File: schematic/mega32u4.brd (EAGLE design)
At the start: 44.4 x 42 mm, 28 parts, among them Q1 16 MHz, T1 BC847, X1 MINI-USB-32005-201

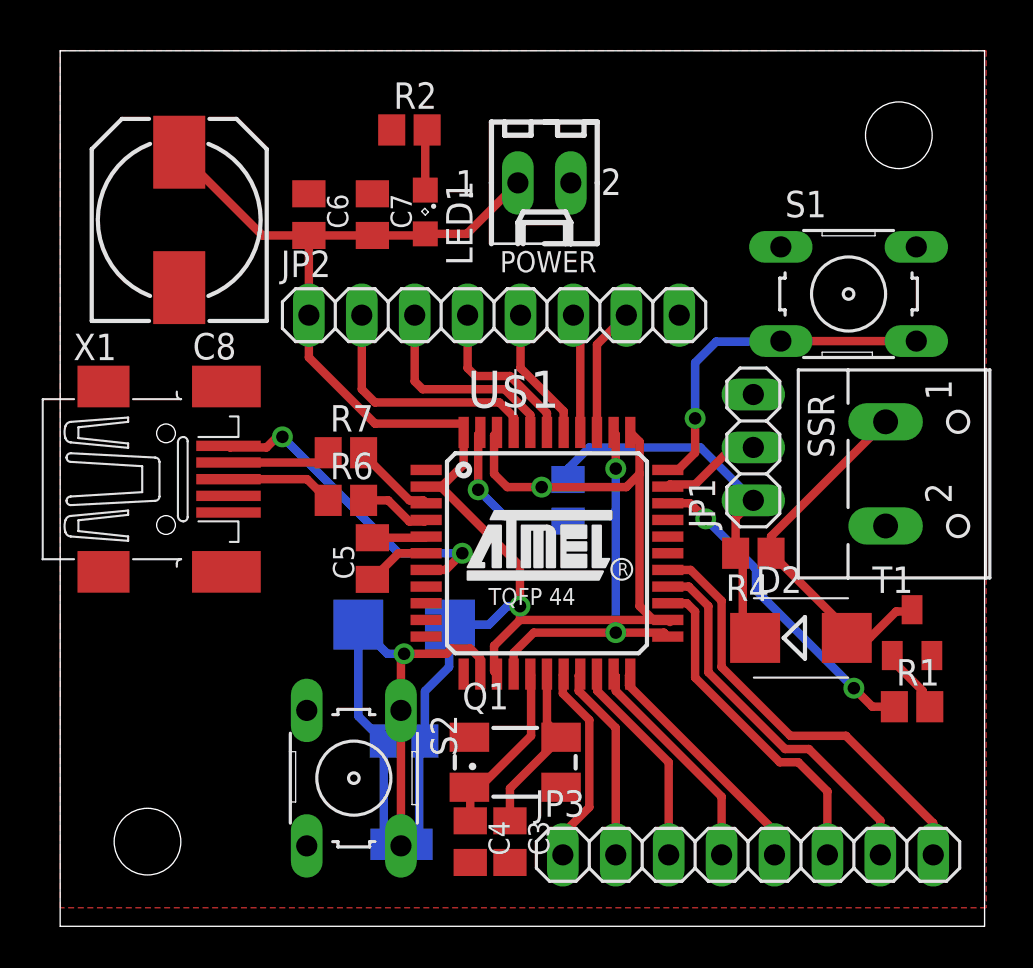
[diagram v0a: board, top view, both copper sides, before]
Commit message: Design Rule Check applied and errors corrected
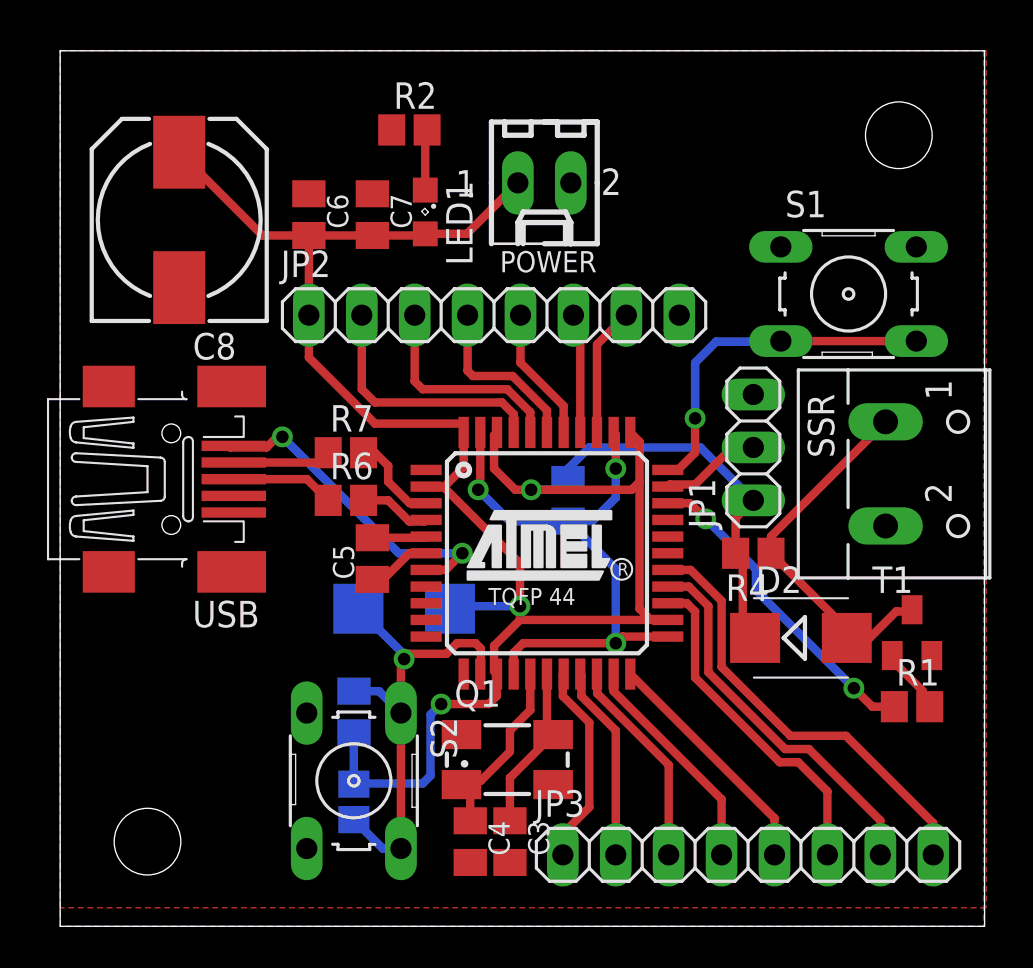
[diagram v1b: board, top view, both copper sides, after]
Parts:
- removed X1: MINI-USB-32005-201, con-cypressindustries:32005-201
- added USB: (no value), con-cypressindustries:32005-201
- U$1: value ATMEGA32U4-AU -> ATMEGA32U4
- moved R5 3.06 mm to (40.3, 24.9), turned to 270 degrees
- moved C1 2.79 mm to (40.3, 29.2), turned to 90 degrees
- moved D1 0.76 mm to (42.7, 34.2)
- moved Q1 0.40 mm to (47.6, 26.9)
- moved S2 0.13 mm to (40.3, 25.9)
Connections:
- removed net N$11: X1.4
- net GND: now also USB.5; no longer X1.5
- net UDM: now also USB.2; no longer X1.2
- net UDP: now also USB.3; no longer X1.3
- net VBUS: now also USB.1; no longer X1.1
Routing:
- net RESET: track 27.8 -> 23.4 mm
- net VCC: track 110.1 -> 112.8 mm, vias 2 -> 3
- net N$3: track 8.63 -> 9.53 mm
- net N$2: track 8.83 -> 8.14 mm
- added copper zone on layer 16, net GND

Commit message: RGB-Led added, pin header repositioned, mounting holes added, ...
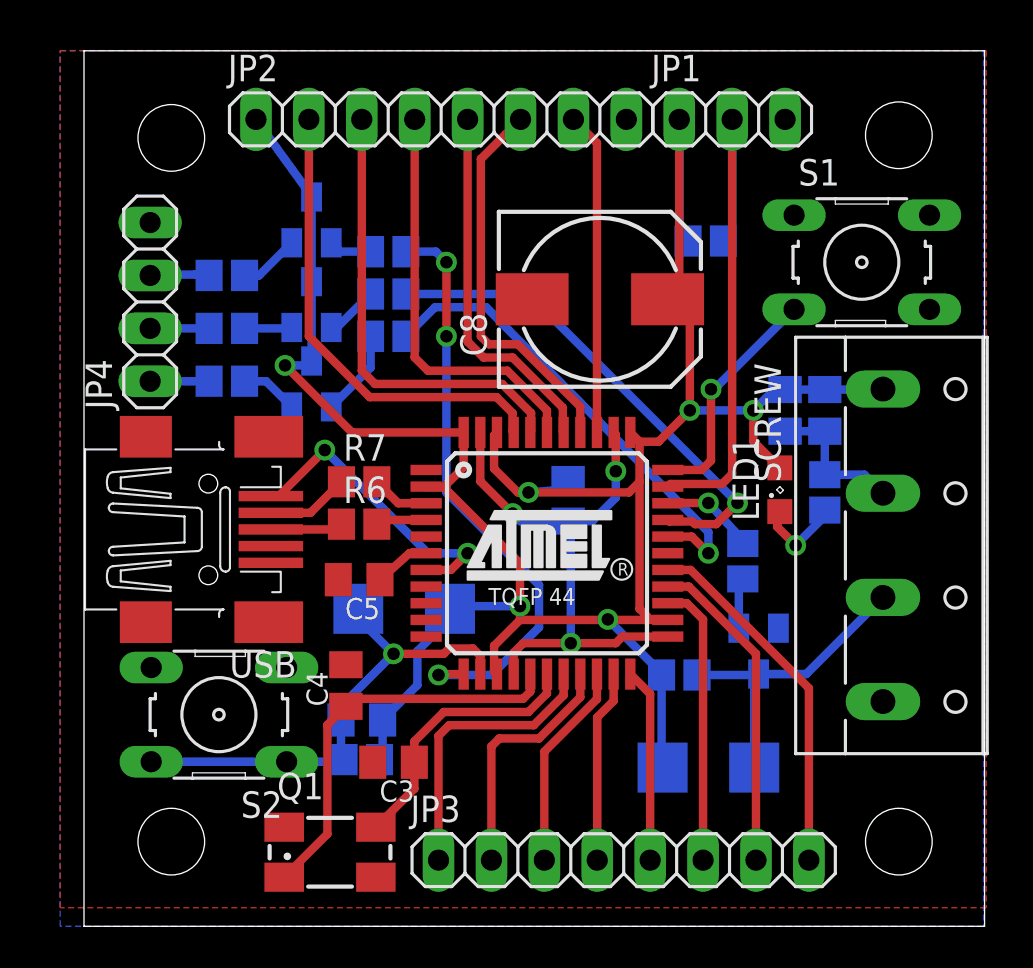
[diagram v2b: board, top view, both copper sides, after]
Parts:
- removed POWER: 22-27-2021-02, con-molex:6410-02
- removed SSR: (no value), con-wago-500:W237-102
- added JP4: (no value), pinhead:1X04
- added R10: 4k7, resistor:R0805
- added R11, R12: 56, resistor:R0805
- added R13: 1k2, resistor:R0805
- added R3, R8, R9: 1k5, resistor:R0805
- added SCREW: (no value), con-wago-500:W237-4
- added T2, T3, T4: (no value), transistor-neu-to92:SOT23-BEC
- R2: value 10K -> 220
- moved C6 26.5 mm to (62.9, 43.7), flipped to the bottom, turned to 90 degrees
- moved R2 26.5 mm to (62.9, 39.8), flipped to the bottom, turned to 270 degrees
- moved C7 21.9 mm to (61.0, 43.7), flipped to the bottom, turned to 90 degrees
- moved LED1 21.6 mm to (60.7, 39.9), turned to 90 degrees
- moved C8 20.5 mm to (52.1, 49.0), turned to 0 degrees
- moved JP1 15.8 mm to (58.4, 57.7), turned to 0 degrees
- moved R1 10.7 mm to (58.9, 36.4), flipped to the bottom, turned to 270 degrees
- moved JP2 9.74 mm to (44.5, 57.7)
- moved Q1 9.60 mm to (39.1, 22.5)
- moved C4 9.58 mm to (39.9, 30.5), turned to 90 degrees
- moved D2 7.65 mm to (57.3, 26.5), flipped to the bottom, turned to 180 degrees
- moved T1 7.42 mm to (59.7, 32.1), flipped to the bottom, turned to 180 degrees
- moved S2 7.21 mm to (33.8, 29.1), turned to 180 degrees
- moved R4 6.84 mm to (55.9, 31.0), flipped to the bottom, turned to 0 degrees
- moved C3 6.76 mm to (42.2, 26.8), turned to 180 degrees
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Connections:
- new net LEDB: R9.2, U$1.12
- new net LEDB_CON: JP4.3, R11.1
- new net LEDG: R3.2, U$1.30
- new net LEDG_CON: JP4.2, R12.1
- new net LEDR: R8.2, U$1.29
- new net LEDR_CON: JP4.1, R13.1
- new net N$11: R9.1, T4.B
- new net N$14: R11.2, T4.E
- new net N$15: R12.2, T3.E
- new net N$16: R13.2, T2.E
- new net N$8: R8.1, T2.B
- new net SSR-VCC: D2.A, R4.1, SCREW.3, T1.3
- net 1WIRE: now also R10.1
- net GND: now also JP4.4, SCREW.2, SCREW.4; no longer POWER.2, SSR.2
- net N$9: now also R3.1, T3.B; no longer D2.A, R4.1, SSR.1, T1.3
- net VCC: now also R10.2, SCREW.1, T2.C, T3.C, T4.C; no longer POWER.1
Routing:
- net LEDB: track 0.00 -> 28.5 mm, vias 0 -> 3
- net LEDG: track 0.00 -> 23.9 mm, vias 0 -> 1
- net LEDR: track 0.00 -> 22.9 mm, vias 0 -> 1
- net 1WIRE: track 4.88 -> 26.4 mm
- net N$9: track 17.9 -> 2.55 mm
- net SSR-VCC: track 0.00 -> 15.0 mm
- net PF6: track 5.77 -> 18.6 mm
- net VCC: track 112.8 -> 125.1 mm, vias 3 -> 6
- net PF1: track 10.3 -> 22.0 mm
- net PF4: track 8.32 -> 19.9 mm
- net PF5: track 6.49 -> 17.8 mm
- net SSR: track 15.5 -> 4.54 mm, vias 2 -> 1
- net PF0: track 12.2 -> 22.7 mm
- net N$3: track 9.53 -> 19.4 mm
- net PF7: track 6.21 -> 15.5 mm
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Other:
- board size 44.4 x 42 mm -> 43.2 x 42 mm

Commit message: Labels modified
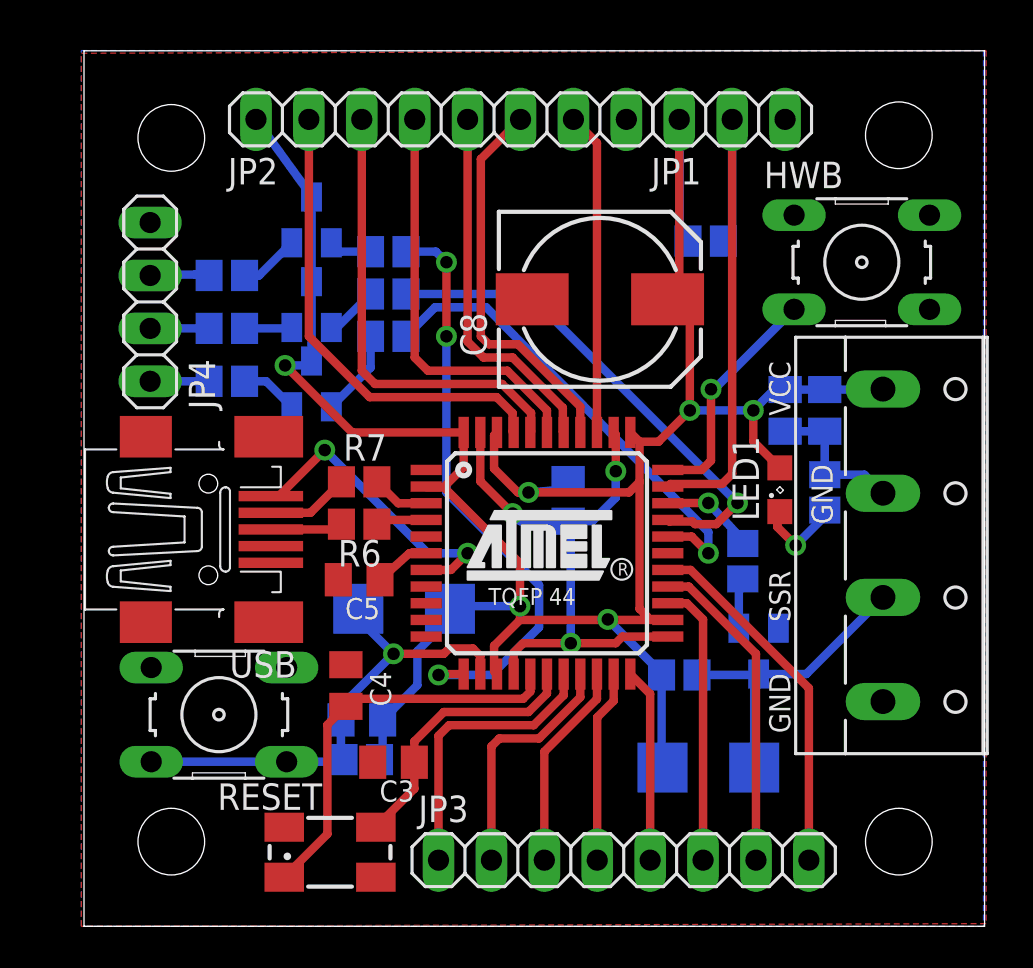
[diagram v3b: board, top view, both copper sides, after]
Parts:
- T1: value BC847 -> (none); device transistor:SOT23 -> transistor-neu-to92:SOT23-BEC
- renumbered S1 to HWB, S2 to RESET
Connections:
- net GND: now also T1.E; no longer T1.2
- net N$5: now also T1.B; no longer T1.1
- net SSR-VCC: now also T1.C; no longer T1.3
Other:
- board text added: "GND"
- board text added: "SSR"
- board text added: "VCC"

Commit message: minor changes
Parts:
- removed LED1: (no value), led:SML0805
- added POWER: (no value), led:SML0805
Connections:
- net N$13: now also POWER.C; no longer LED1.C
- net VCC: now also POWER.A; no longer LED1.A
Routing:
- net N$10: track 11.3 -> 17.8 mm
- net N$13: track 4.23 -> 6.38 mm
- net GND: vias 0 -> 1
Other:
- board text added: "+5V"
- board text added: "ChaosCoffeeControl"
- board text added: "v0.1"
- board text removed: "VCC"
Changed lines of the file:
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@@
 <layer number="45" name="Holes" color="7" fill="1" visible="yes" active="yes"/>
 <layer number="46" name="Milling" color="3" fill="1" visible="no" active="yes"/>
-<layer number="47" name="Measures" color="7" fill="1" visible="no" active="yes"/>
+<layer number="47" name="Measures" color="7" fill="1" visible="yes" active="yes"/>
 <layer number="48" name="Document" color="7" fill="1" visible="yes" active="yes"/>
 <layer number="49" name="Reference" color="7" fill="1" visible="yes" active="yes"/>
@@
 <hole x="31.496" y="56.769" drill="3.2"/>
 <hole x="66.421" y="22.987" drill="3.2"/>
-<dimension x1="27.305" y1="60.95" x2="27.305" y2="18.923" x3="22.86" y3="39.9365" layer="1"/>
-<dimension x1="27.305" y1="18.923" x2="70.536" y2="18.923" x3="48.9205" y3="63.246" layer="1"/>
-<text x="61.214" y="43.434" size="1.016" layer="25" rot="R90">VCC</text>
+<dimension x1="27.305" y1="60.95" x2="27.305" y2="18.923" x3="22.86" y3="39.9365" layer="47"/>
+<dimension x1="27.305" y1="18.923" x2="70.536" y2="18.923" x3="48.9205" y3="63.246" layer="47"/>
+<text x="61.214" y="43.942" size="1.016" layer="25" rot="R90">+5V</text>
 <text x="61.214" y="28.194" size="1.016" layer="25" rot="R90">GND</text>
 <text x="61.214" y="33.528" size="1.016" layer="25" rot="R90">SSR</text>
-<text x="63.246" y="38.227" size="1.016" layer="25" rot="R90">GND</text>
+<text x="61.214" y="36.957" size="1.016" layer="25" rot="R90">GND</text>
+<text x="46.609" y="25.4" size="1.27" layer="51">ChaosCoffeeControl</text>
+<text x="52.705" y="24.13" size="1.016" layer="51">v0.1</text>
 </plain>
 <attributes>
@@
 </autorouter>
 <elements>
-<element name="U$1" library="mega32U4" package="TQFP44" value="ATMEGA32U4" x="49.53" y="36.83" smashed="yes">
-<attribute name="VALUE" x="43.688" y="43.6959" size="1.27" layer="27"/>
-</element>
+<element name="U$1" library="mega32U4" package="TQFP44" value="ATMEGA32U4" x="49.53" y="36.83" smashed="yes"/>
 <element name="C1" library="resistor" package="C0805K" value="47nF" x="40.64" y="28.829" smashed="yes" rot="MR0">
 <attribute name="NAME" x="41.64" y="29.704" size="1.016" layer="26" rot="MR0"/>
@@
 <attribute name="MF" value="" x="39.116" y="22.479" size="1.778" layer="27" display="off"/>
 <attribute name="OC_FARNELL" value="unknown" x="39.116" y="22.479" size="1.778" layer="27" display="off"/>
-<attribute name="VALUE" x="35.814" y="21.844" size="1.27" layer="27"/>
 </element>
 <element name="USB" library="con-cypressindustries" package="32005-201" value="" x="33.274" y="37.973" smashed="yes">
@@
 <attribute name="MF" value="" x="33.274" y="37.973" size="1.778" layer="27" display="off"/>
 <attribute name="OC_FARNELL" value="unknown" x="33.274" y="37.973" size="1.778" layer="27" display="off"/>
-<attribute name="NAME" x="34.29" y="30.861" size="1.27" layer="25"/>
+<attribute name="NAME" x="31.369" y="32.385" size="1.27" layer="25"/>
 <attribute name="VALUE" x="28.829" y="30.988" size="1.27" layer="27"/>
 </element>
@@
 <attribute name="MF" value="" x="33.782" y="29.083" size="1.778" layer="27" rot="R180" display="off"/>
 <attribute name="OC_FARNELL" value="176432" x="33.782" y="29.083" size="1.778" layer="27" rot="R180" display="off"/>
-<attribute name="NAME" x="38.735" y="25.781" size="1.27" layer="25" ratio="10" rot="R180"/>
+<attribute name="NAME" x="39.37" y="25.781" size="1.27" layer="25" ratio="10" rot="R180"/>
 <attribute name="VALUE" x="36.83" y="34.163" size="1.27" layer="27" ratio="10" rot="R180"/>
 </element>
@@
 <attribute name="NAME" x="63.74" y="42.688" size="1.016" layer="26" rot="MR90"/>
 </element>
-<element name="LED1" library="led" package="SML0805" value="" x="60.706" y="39.878" rot="R90"/>
+<element name="POWER" library="led" package="SML0805" value="" x="60.706" y="42.037" smashed="yes" rot="R90">
+<attribute name="NAME" x="59.706" y="39.267" size="1.27" layer="25" rot="R90"/>
+<attribute name="VALUE" x="62.706" y="40.537" size="1.27" layer="27" rot="R90"/>
+</element>
 <element name="C8" library="resistor" package="150CLZ-0810" value="470uF" x="52.07" y="49.022"/>
 <element name="C7" library="resistor" package="C0805K" value="330nF" x="60.96" y="43.688" smashed="yes" rot="MR90">
@@
 <wire x1="50.292" y1="39.878" x2="48.641" y2="39.751" width="0.4064" layer="16"/>
 <via x="48.641" y="39.751" extent="1-16" drill="0.6"/>
-<contactref element="LED1" pad="A"/>
+<contactref element="POWER" pad="A"/>
 <contactref element="C8" pad="+"/>
 <contactref element="C6" pad="2"/>
@@
 <via x="59.436" y="43.688" extent="1-16" drill="0.6"/>
 <wire x1="59.436" y1="43.688" x2="59.436" y2="42.198" width="0.4064" layer="1"/>
-<wire x1="59.436" y1="42.198" x2="60.706" y2="40.928" width="0.4064" layer="1"/>
+<wire x1="59.436" y1="42.198" x2="60.706" y2="43.087" width="0.4064" layer="1"/>
 <wire x1="60.96" y1="44.688" x2="60.436" y2="44.688" width="0.4064" layer="16"/>
 <wire x1="59.436" y1="43.688" x2="56.388" y2="43.688" width="0.4064" layer="16"/>
@@
 <contactref element="JP4" pad="4"/>
 <contactref element="T1" pad="E"/>
+<via x="52.451" y="36.068" extent="1-16" drill="0.6"/>
 </signal>
 <signal name="N$4">
@@
 <wire x1="57.404" y1="44.704" x2="57.5564" y2="44.704" width="0.4064" layer="16"/>
 <wire x1="57.5564" y1="44.704" x2="61.3918" y2="48.5394" width="0.4064" layer="16"/>
-<wire x1="61.3918" y1="48.5394" x2="67.8942" y2="48.5394" width="0" layer="19" extent="1-1"/>
+<wire x1="61.3918" y1="48.5394" x2="67.8942" y2="48.5394" width="0.4064" layer="16"/>
 </signal>
 <signal name="PF7">
@@
 <signal name="N$13">
 <contactref element="R2" pad="2"/>
-<contactref element="LED1" pad="C"/>
-<wire x1="60.706" y1="38.828" x2="60.579" y2="38.1" width="0.4064" layer="1"/>
+<contactref element="POWER" pad="C"/>
+<wire x1="60.706" y1="40.987" x2="60.579" y2="38.1" width="0.4064" layer="1"/>
 <wire x1="60.579" y1="38.1" x2="61.468" y2="37.211" width="0.4064" layer="1"/>
 <via x="61.468" y="37.211" extent="1-16" drill="0.6"/>
@@
 </signal>
 </signals>
-<errors>
-</errors>
 </board>
 </drawing>

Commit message: bug fixes
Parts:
- added TP1, TP2, TP3, TP4: TPTP10R, testpad:TP10R
- moved C4 2.27 mm to (41.9, 29.5), turned to 270 degrees
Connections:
- new net N$12: TP2.TP, U$1.10
- new net N$17: TP3.TP, U$1.11
- net GND: now also C2.2, U$1.15, U$1.23, U$1.35, U$1.43
- net N$1: now also TP1.TP, U$1.9; no longer C2.2, U$1.15, U$1.23, U$1.35, U$1.43
- net RESET: now also TP4.TP
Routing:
- net N$1: track 28.5 -> 3.89 mm, vias 3 -> 0
- net GND: track 7.15 -> 12.2 mm
- net RESET: track 23.6 -> 28.3 mm
- net N$17: track 0.00 -> 4.33 mm
- net N$12: track 0.00 -> 4.08 mm
- net VCC: track 124.8 -> 123.9 mm
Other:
- board text added: "v0.2"
- board text removed: "v0.1"
